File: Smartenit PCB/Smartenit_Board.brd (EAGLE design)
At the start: 54.9 x 71.8 mm, 86 parts, among them J1 2X5CONNECTOR1.27MM, Q1 QUARTZ_3.58M_2PIN, U1 SN74LVC1G3157, U2 ADE7953, U3 ESP-WROOM-32

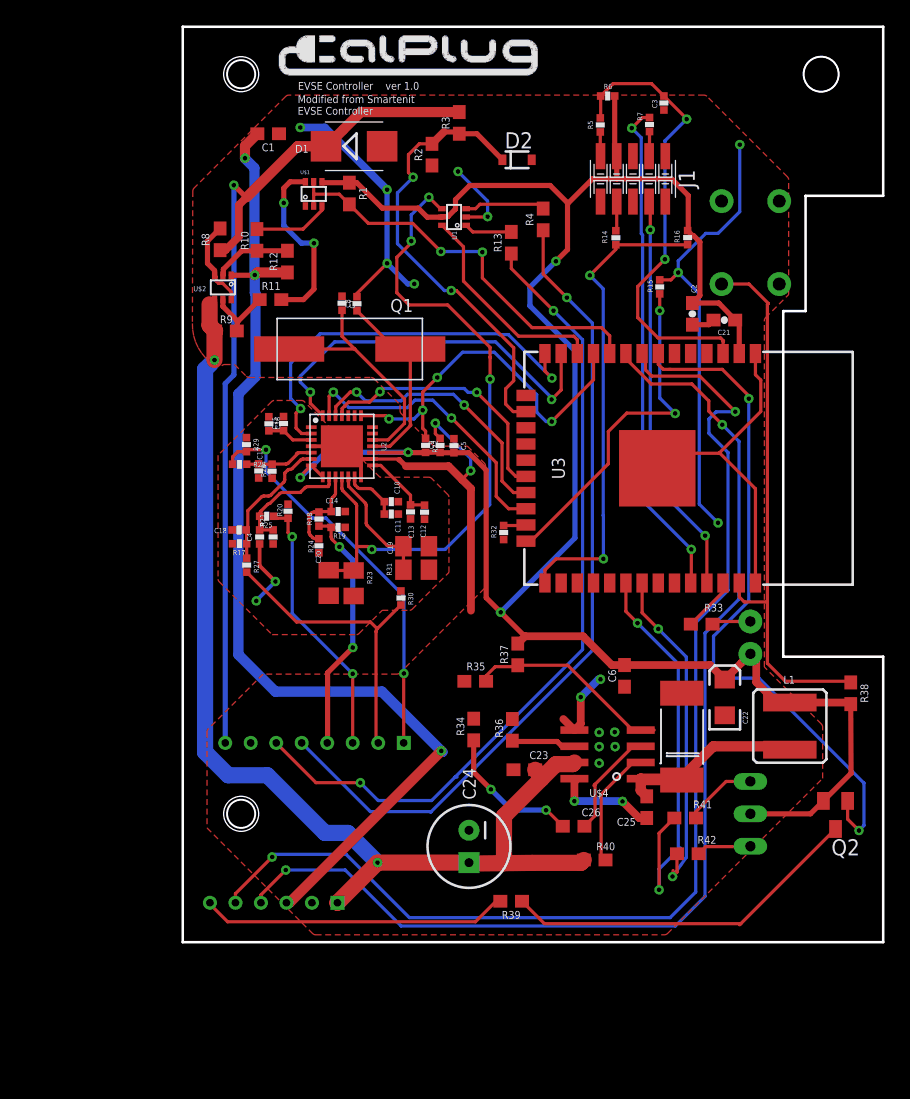
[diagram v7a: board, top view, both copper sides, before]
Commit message: Additional Modifications from Al
-moved mplex to connector region
-fixed ground connections to match Als exactly
-additional reogranization of traces
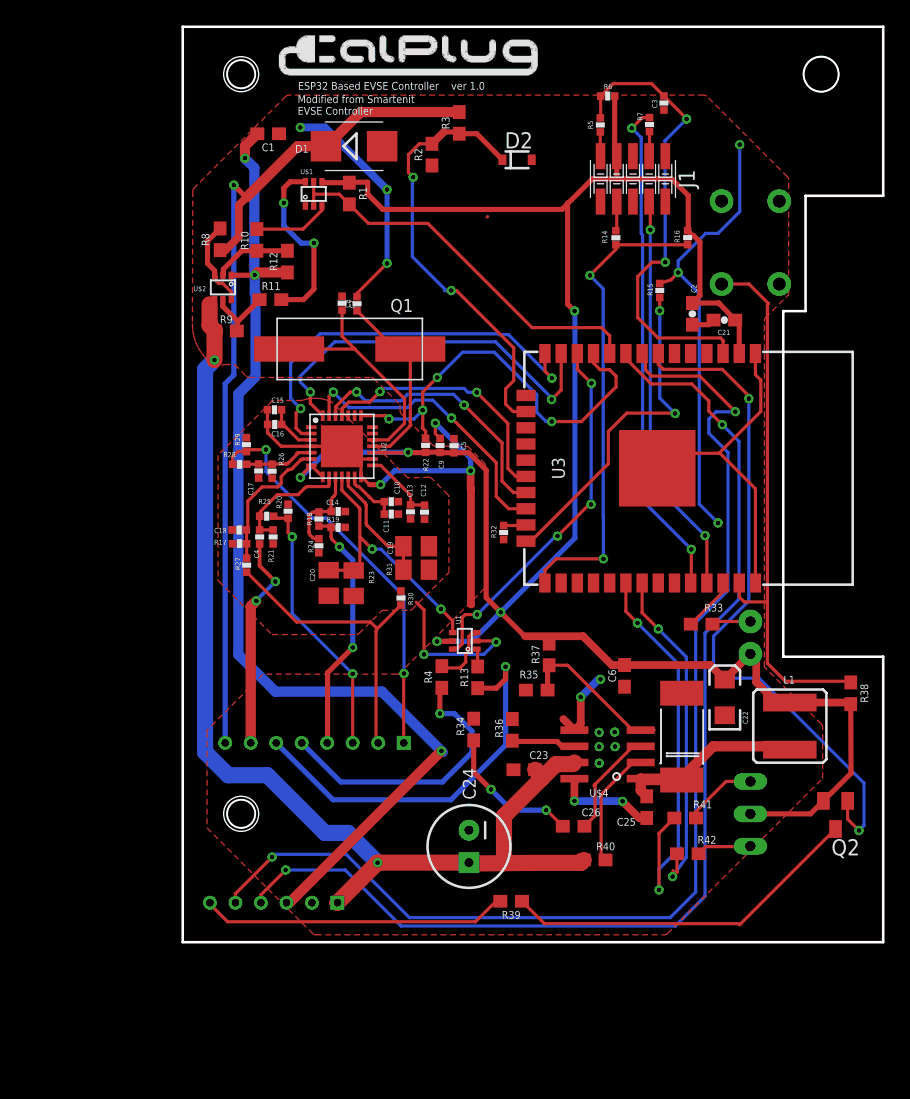
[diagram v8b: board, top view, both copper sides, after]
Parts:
- moved R4 36.8 mm to (20.3, -51.0)
- moved R13 34.2 mm to (23.1, -51.0)
- moved U1 33.3 mm to (23.1, -48.8)
- moved R35 4.87 mm to (27.8, -52.0)
- moved R37 2.46 mm to (28.7, -49.2)
- moved C15 1.29 mm to (7.20, -30.0), turned to 0 degrees
- moved C16 0.46 mm to (7.21, -31.2), turned to 0 degrees
- moved R15 0.28 mm to (37.4, -20.7)
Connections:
- net AGND: now also C10.2, C11.2, C12.1, C13.1, C14.2, C17.1, C18.2, C19.2, C20.2, C4.1, R17.2, R19.2, R20.1, R21.1, R23.2, R24.2, R26.1, R29.1, R30.2, R31.2; no longer C1.1, C2.2, C21.2, C22.C, C23.1, C24.2, C3.1, C5.1, C6.1, C7.1, C8.1, C9.1, D1.A, D2.2, D3.P, J1.10, R15.1, R2.1, R32.1, R34.1, R35.1, R36.1, S100.1, U$1.1, U$4.5, U$5.5, U2.14, U3.1, U3.15, U3.38, U3.GND
- net DGND: now also C1.1, C2.2, C21.2, C22.C, C23.1, C24.2, C3.1, C5.1, C6.1, C7.1, C8.1, C9.1, D1.A, D2.2, D3.P, J1.10, R15.1, R2.1, R32.1, R34.1, R35.1, R36.1, S100.1, U$1.1, U$4.5, U$5.5, U2.14, U3.1, U3.15, U3.38, U3.GND; no longer C10.2, C11.2, C12.1, C13.1, C14.2, C17.1, C18.2, C19.2, C20.2, C4.1, R17.2, R19.2, R20.1, R21.1, R23.2, R24.2, R26.1, R29.1, R30.2, R31.2
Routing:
- net DGND: track 8.00 -> 125.2 mm, vias 2 -> 11
- net AGND: track 125.0 -> 30.3 mm, vias 13 -> 4
- net LNV1: track 64.9 -> 22.4 mm
- net LNV2: track 64.3 -> 31.2 mm, vias 2 -> 1
- net N$3: track 53.8 -> 21.8 mm, vias 4 -> 2
- net MPLEX: track 17.0 -> 29.1 mm, vias 0 -> 4
- net 3.3V: track 175.2 -> 179.7 mm, vias 4 -> 5
- net N$19: track 16.1 -> 12.5 mm
- net DIO5: track 30.3 -> 33.5 mm
- net N$54: track 3.76 -> 1.38 mm
- net N$55: track 6.37 -> 5.00 mm
- net PILOT_GEN: track 32.7 -> 31.5 mm, vias 2 -> 0
- net NRST: track 35.8 -> 36.4 mm
- net PILOT_READ: track 35.9 -> 35.4 mm
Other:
- board text added: "ESP32 Based EVSE Controller ver 1.0"
- board text removed: "EVSE Controller ver 1.0"
